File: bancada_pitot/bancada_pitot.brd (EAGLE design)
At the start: 99 x 54.3 mm, 18 parts, among them X1 22-23-2041, X2 22-23-2041

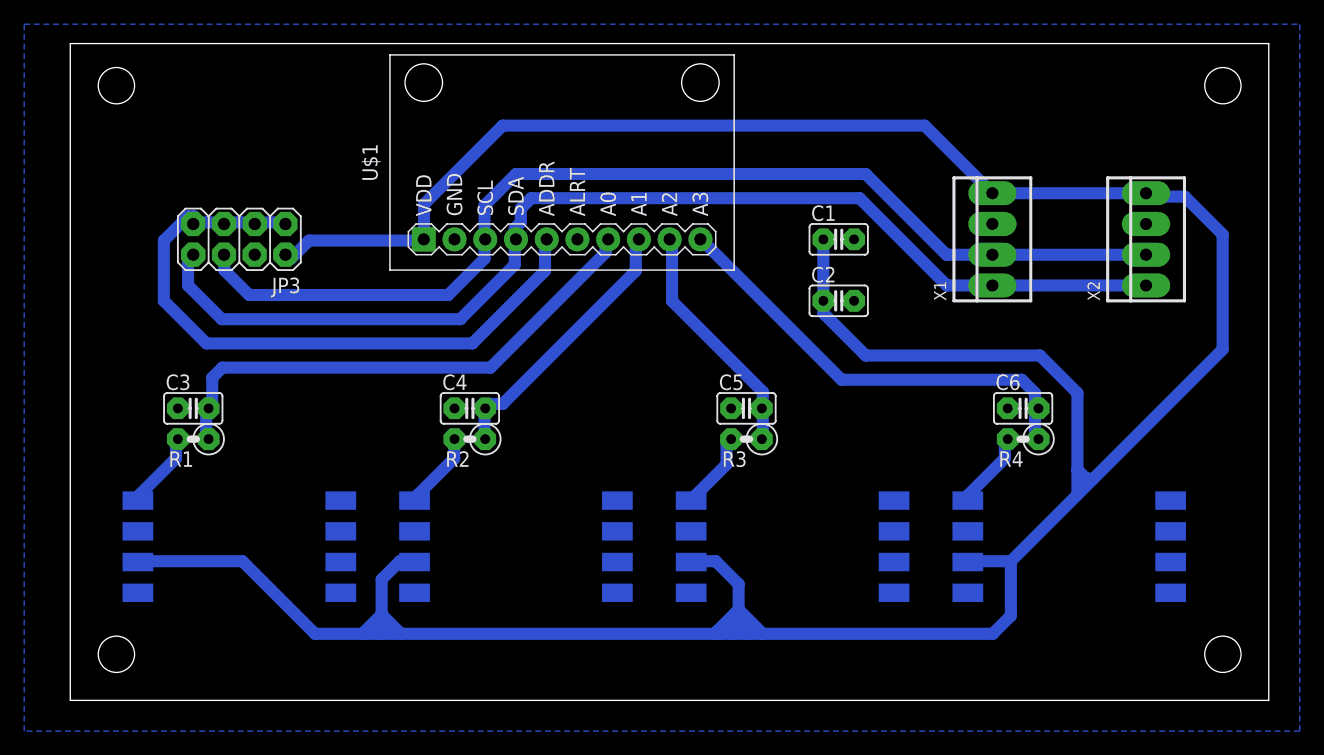
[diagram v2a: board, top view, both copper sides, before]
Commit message: Correct position for edge lines
Both top and right edge lines were bad positioned, in a way that the four board holes were not the same distance from the edges. This makes dificult to position them on CAD files for posterior case modeling.

Now the holes are 150mil apart from each edge.
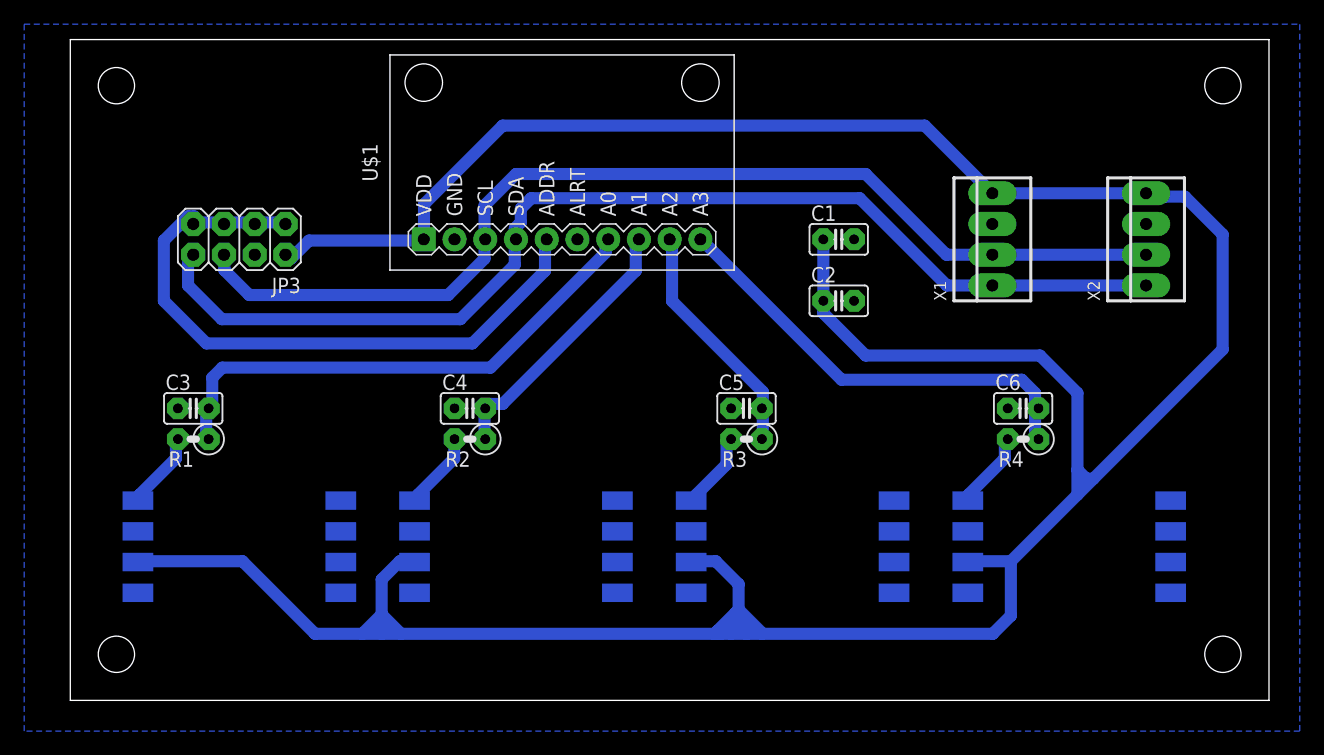
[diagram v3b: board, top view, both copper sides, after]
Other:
- board size 99 x 54.3 mm -> 99.1 x 54.6 mm
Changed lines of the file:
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@@
 <?xml version="1.0" encoding="utf-8"?>
 <!DOCTYPE eagle SYSTEM "eagle.dtd">
-<eagle version="8.6.0">
+<eagle version="9.0.0">
 <drawing>
 <settings>
@@
 <setting verticaltext="up"/>
 </settings>
-<grid distance="50" unitdist="mil" unit="mm" style="lines" multiple="1" display="no" altdistance="5" altunitdist="mil" altunit="mil"/>
+<grid distance="50" unitdist="mil" unit="mil" style="lines" multiple="1" display="no" altdistance="5" altunitdist="mil" altunit="mil"/>
 <layers>
 <layer number="1" name="Top" color="4" fill="1" visible="yes" active="yes"/>
@@
 <board>
 <plain>
-<wire x1="0" y1="0" x2="99.04" y2="0" width="0" layer="20"/>
-<wire x1="99.04" y1="0" x2="99.04" y2="54.28" width="0" layer="20"/>
-<wire x1="99.04" y1="54.28" x2="0" y2="54.28" width="0" layer="20"/>
-<wire x1="0" y1="54.28" x2="0" y2="0" width="0" layer="20"/>
+<wire x1="0" y1="0" x2="99.06" y2="0" width="0" layer="20"/>
+<wire x1="99.06" y1="0" x2="99.06" y2="54.61" width="0" layer="20"/>
+<wire x1="99.06" y1="54.61" x2="0" y2="54.61" width="0" layer="20"/>
+<wire x1="0" y1="54.61" x2="0" y2="0" width="0" layer="20"/>
 <hole x="3.81" y="50.8" drill="3"/>
 <hole x="3.81" y="3.81" drill="3"/>

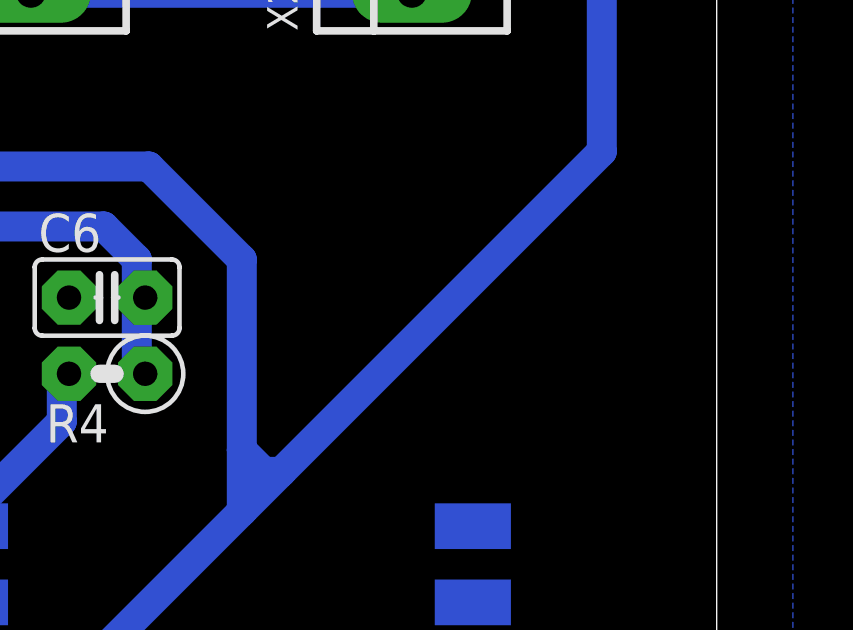
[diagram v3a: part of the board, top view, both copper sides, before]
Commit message: Add jumpers (or 0ohm resistors)
In previous design, some ground planes were unconnected to each other. It was meant to be added jumper wires after production.

This commit changes this to actual jumpers, with pins, so they don't need to be soldered from bottom, but can actually be placed on top, like any other through-hole component. 0ohm through-hole resistors can also be used.
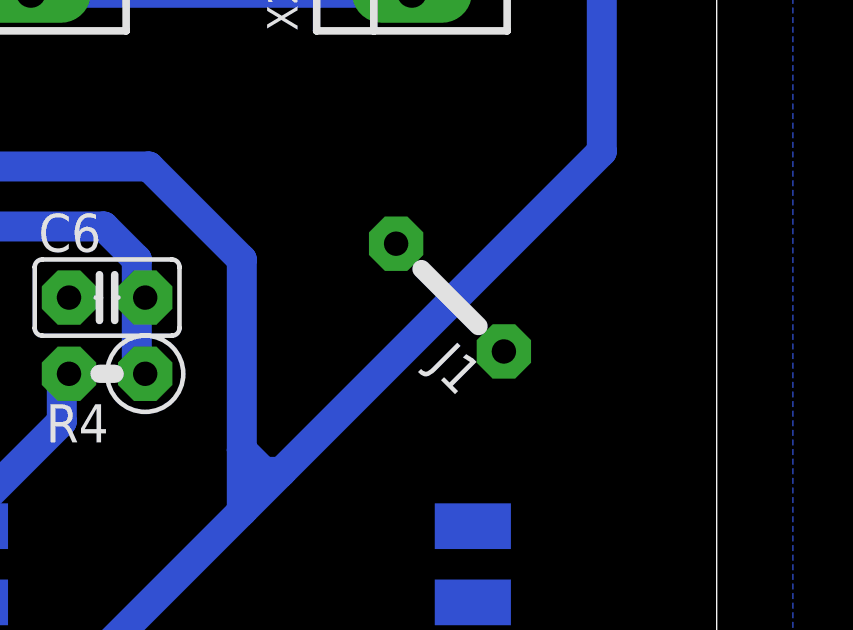
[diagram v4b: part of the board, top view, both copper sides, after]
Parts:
- added J1: J5MM, jumper:05
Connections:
- net GND: now also J1.1, J1.2
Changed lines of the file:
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@@
 </element>
 <element name="JP3" library="pinhead" library_urn="urn:adsk.eagle:library:325" package="2X04" package3d_urn="urn:adsk.eagle:package:22461/2" value="" x="13.97" y="38.1" rot="R180"/>
+<element name="J1" library="jumper" library_urn="urn:adsk.eagle:library:252" package="05" package3d_urn="urn:adsk.eagle:package:15465/1" value="J5MM" x="90.17" y="24.13" rot="R135"/>
 </elements>
 <signals>
@@
 <contactref element="X2" pad="3"/>
 <contactref element="JP3" pad="4"/>
-<wire x1="54.61" y1="24.13" x2="64.77" y2="33.02" width="0" layer="19" extent="1-1"/>
+<contactref element="J1" pad="2"/>
+<contactref element="J1" pad="1"/>
+<wire x1="91.96605" y1="22.333946875" x2="88.373946875" y2="25.92605" width="0" layer="19" extent="1-1"/>
 </signal>
 <signal name="A0">
@@
 </signal>
 </signals>
+<errors>
+</errors>
 </board>
 </drawing>

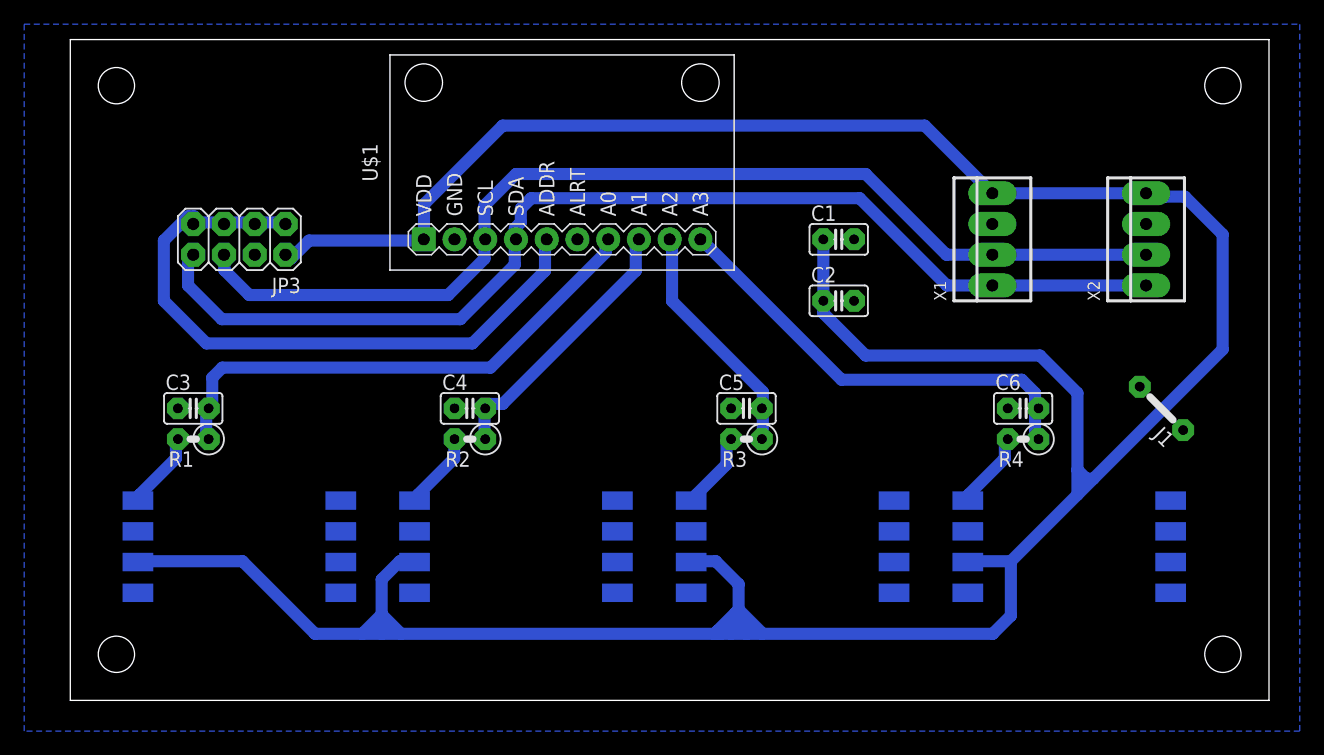
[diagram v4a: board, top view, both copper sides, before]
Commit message: Change board edges and holes
Edges and holes are supossed to be in "mm", different from the components and traces, that should follow "mil" units. 

This way we the board respects the board manufacturer (who uses mil system) as well as the CAD designer (who uses metric system).
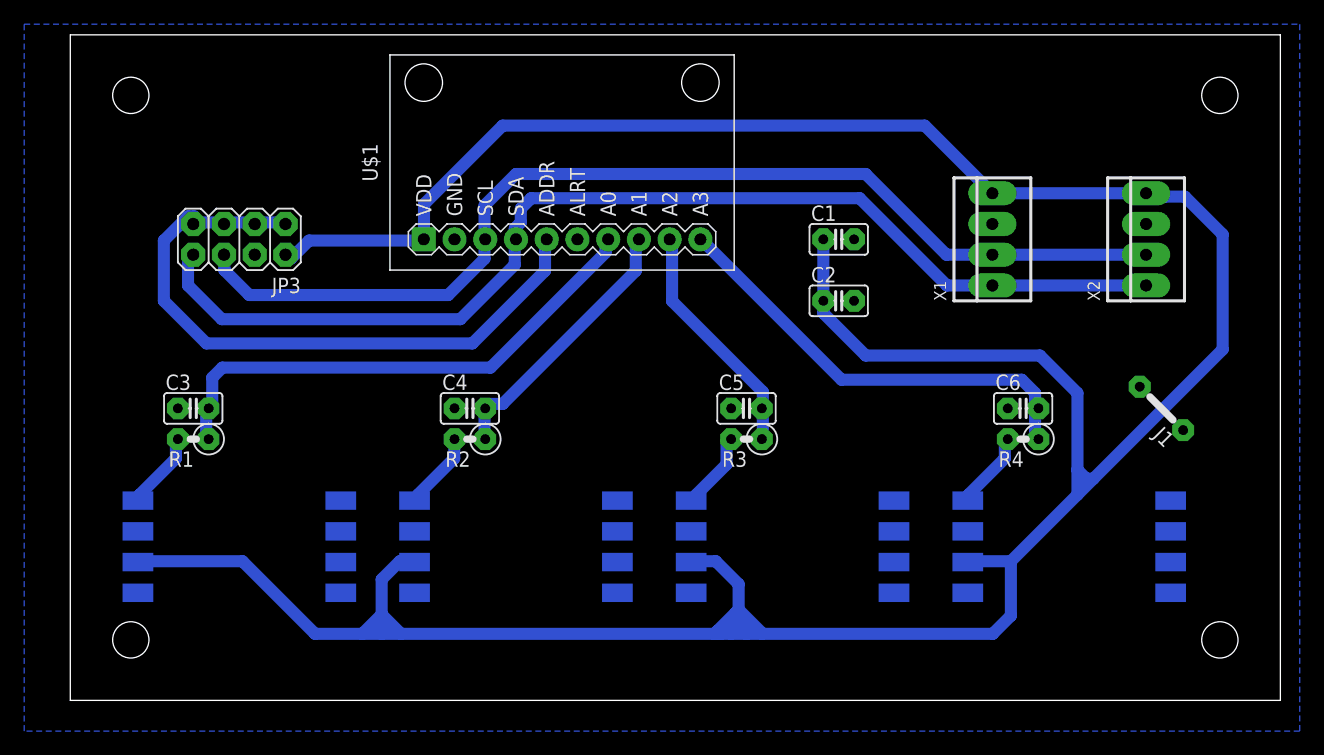
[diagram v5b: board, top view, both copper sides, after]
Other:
- board size 99.1 x 54.6 mm -> 100 x 55 mm
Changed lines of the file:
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@@
 <setting verticaltext="up"/>
 </settings>
-<grid distance="50" unitdist="mil" unit="mil" style="lines" multiple="1" display="no" altdistance="5" altunitdist="mil" altunit="mil"/>
+<grid distance="40" unitdist="mil" unit="mil" style="lines" multiple="1" display="no" altdistance="5" altunitdist="mil" altunit="mil"/>
 <layers>
 <layer number="1" name="Top" color="4" fill="1" visible="yes" active="yes"/>
@@
 <board>
 <plain>
-<wire x1="0" y1="0" x2="99.06" y2="0" width="0" layer="20"/>
-<wire x1="99.06" y1="0" x2="99.06" y2="54.61" width="0" layer="20"/>
-<wire x1="99.06" y1="54.61" x2="0" y2="54.61" width="0" layer="20"/>
-<wire x1="0" y1="54.61" x2="0" y2="0" width="0" layer="20"/>
-<hole x="3.81" y="50.8" drill="3"/>
-<hole x="3.81" y="3.81" drill="3"/>
-<hole x="95.25" y="50.8" drill="3"/>
-<hole x="95.25" y="3.81" drill="3"/>
+<wire x1="0" y1="0" x2="100" y2="0" width="0" layer="20"/>
+<wire x1="100" y1="0" x2="100" y2="55" width="0" layer="20"/>
+<wire x1="100" y1="55" x2="0" y2="55" width="0" layer="20"/>
+<wire x1="0" y1="55" x2="0" y2="0" width="0" layer="20"/>
+<hole x="5" y="50" drill="3"/>
+<hole x="5" y="5" drill="3"/>
+<hole x="95" y="50" drill="3"/>
+<hole x="95" y="5" drill="3"/>
 </plain>
 <attributes>
